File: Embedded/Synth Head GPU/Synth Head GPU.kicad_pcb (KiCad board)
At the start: 2 copper layers, 60 x 25 mm, 56 parts, among them J1 10171746-00021LF, J2 JST [D], J3 JST [D], J4 JST [G], U1 ICM-20948, U10 FFC [G], U11 SRV05-4, U12 AP7366-W5-7, U13 TCA9535RTWR, U14 AP7366-33W5-7, U2 BME280, U3 MCP7940N-xSN, U4 MP05346, U5 FFC [D], U6 FFC [D], U7 FFC [C], U8 FFC [C], U9 FFC [U]

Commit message: Prepared Circuits for Routing and Placement Tuning
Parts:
- removed BT1: BH-25C-1, Battery_BH25C-1:BAT_BH-25C-1
- removed D2: WL-SMCW_0603, LED_Red_SMD:WL-SMCW_0603
- added J5: Coin Cell, Connector_PinHeader_2.54mm:PinHeader_1x02_P2.54mm_Vertical, F.Cu at (143.2, 87.0)
- BootSW1, C10, C11, C6, C7, C8, ESP1, J1, J4, R2, R3, R4, U3, U4, U5, U6, U7, U8, U9: moved to B.Cu
- moved C5 71.9 mm to (164.0, 91.0)
- moved C4 69.7 mm to (161.5, 88.5), turned to 90 degrees
- moved U2 68.6 mm to (164.0, 88.5)
- moved C11 59.7 mm to (172.5, 87.5), turned to 90 degrees
- moved R1 56.8 mm to (168.5, 91.0)
- moved C9 54.9 mm to (168.5, 89.5)
- moved U5 54.5 mm to (174.7, 102.5), turned to -90 degrees
- moved J2 54.4 mm to (176.3, 104.4), turned to 90 degrees
- moved ESP1 53.6 mm to (161.5, 95.5), turned to 180 degrees
- moved R11 49.7 mm to (158.6, 95.0), turned to 180 degrees
- moved U9 46.0 mm to (167.5, 110.0), turned to 180 degrees
- moved C17 44.0 mm to (157.6, 98.0), turned to 180 degrees
- moved J4 42.3 mm to (141.1, 111.6), turned to -90 degrees
- moved C10 40.5 mm to (174.0, 87.5), turned to 90 degrees
- moved U7 38.6 mm to (174.7, 91.0), turned to -90 degrees
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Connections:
- U13 pad 5: UI IO 0 -> XShut 0
- U13 pad 6: UI IO 1 -> XShut 1
- U5 pad 10: Disp TX -> Disp 0 TX
- U5 pad 12: Disp 6 -> Disp 5
- U5 pad 13: Disp 7 -> Disp 4
- U5 pad 14: Disp 8 -> Disp 3
- U5 pad 15: Disp 9 -> Disp 2
- U5 pad 16: Disp 10 -> Disp 1
- U5 pad 17: Disp 11 -> Disp 0
- U5 pad 2: Disp 0 -> Disp 11
- U5 pad 3: Disp 1 -> Disp 10
- U5 pad 4: Disp 2 -> Disp 9
- U5 pad 5: Disp 3 -> Disp 8
- U5 pad 6: Disp 4 -> Disp 7
- U5 pad 7: Disp 5 -> Disp 6
- U5 pad 9: Disp RX -> Disp 0 RX
- U6 pad 10: Disp TX -> Disp 1 TX
- U6 pad 9: Disp RX -> Disp 1 RX

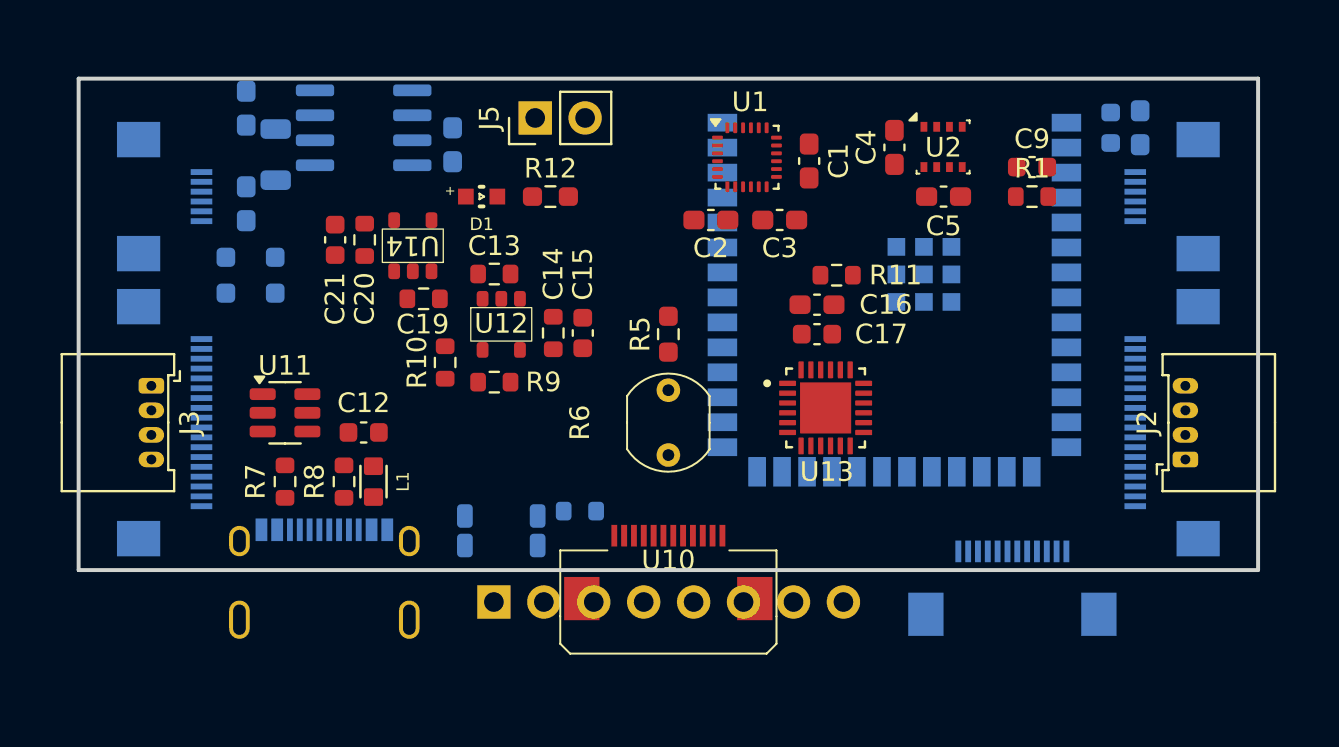
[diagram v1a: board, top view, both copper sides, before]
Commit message: GPU Routed All but pins to ESP32
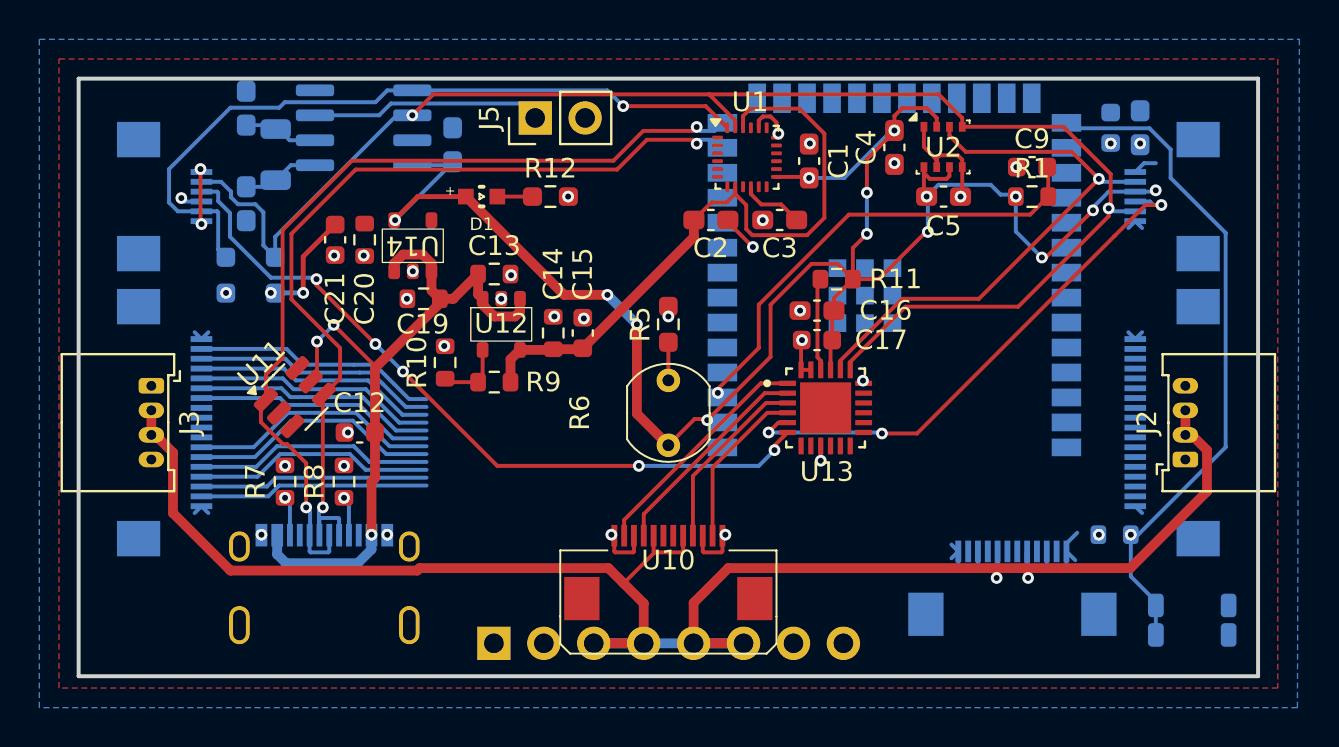
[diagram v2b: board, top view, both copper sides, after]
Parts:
- removed L1: MPZ1608S601ATA00, Ferrite_Bead_MPZ1608S601ATA00:INDC1608X95N
- moved BootSW1 35.4 mm to (176.7, 112.5), turned to 0 degrees
- moved R2 27.2 mm to (172.7, 108.2), turned to 0 degrees
- moved J4 2.10 mm to (141.1, 113.7)
- moved U11 0.94 mm to (131.0, 101.2), turned to 45 degrees
- moved R5 0.50 mm to (150.0, 97.5)
- moved R6 0.50 mm to (150.0, 102.0)
- moved C16 0.30 mm to (157.6, 96.8)
- moved C17 0.30 mm to (157.6, 98.3)
- moved J1 0.27 mm to (132.5, 112.8)
- moved R11 0.20 mm to (158.6, 95.2)
- moved C12 0.20 mm to (134.3, 103.0)
- turned ESP1 to 0 degrees
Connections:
- C12 pad 1: /1V8 Regulator/Vin -> +5V
- C13 pad 1: /1V8 Regulator/Vin -> +5V
- C19 pad 1: /1V8 Regulator/Vin -> +5V
- J1 pad A4_B9: Net-(J1-VBUS_A) -> +5V
- J1 pad B4_A9: Net-(J1-VBUS_A) -> +5V
- U12 pad 1: /1V8 Regulator/Vin -> +5V
- U12 pad 3: /1V8 Regulator/Vin -> +5V
- U14 pad 1: /1V8 Regulator/Vin -> +5V
- U14 pad 3: /1V8 Regulator/Vin -> +5V
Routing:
- net +5V: track 0.00 -> 129.5 mm, vias 0 -> 5
- net +3V3: track 0.00 -> 102.5 mm, vias 0 -> 21
- net SCL: track 0.00 -> 77.5 mm, vias 0 -> 2
- net SDA: track 0.00 -> 65.7 mm, vias 0 -> 2
- net USB +: track 0.00 -> 44.6 mm, vias 0 -> 2
- net USB -: track 0.00 -> 43.7 mm, vias 0 -> 2
- net XShut 1: track 0.00 -> 37.6 mm, vias 0 -> 5
- net GND: track 0.00 -> 36.6 mm, vias 0 -> 31
- net Net-(ESP1-GPIO0/BOOT): track 0.00 -> 34.5 mm, vias 0 -> 1
- net +1V8: track 0.00 -> 33.1 mm
- net XShut 0: track 0.00 -> 27.4 mm, vias 0 -> 3
- net Net-(ESP1-EN): track 0.00 -> 23.9 mm, vias 0 -> 1
- net Disp 4: track 0.00 -> 12.9 mm
- net Disp 5: track 0.00 -> 12.9 mm
- net Disp 11: track 0.00 -> 12.5 mm
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- added copper zone on F.Cu, net +3V3
- added copper zone on B.Cu, net GND
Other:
- board size 60 x 25 mm -> 60 x 30.4 mm
